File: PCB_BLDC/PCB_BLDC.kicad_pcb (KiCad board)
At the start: 2 copper layers, 181.9 x 138.4 mm, 61 parts, among them J10 Conn_01x06, J11 Conn_01x07, J12 Conn_01x06, J13 Conn_01x08, J16 Conn_01x08, J17 Conn_01x10, J8 VCC_Unregulated, J9 VCC_GND, Q1 IRF4905, SW1 Rotary_Encoder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

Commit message: Main: Finish PCB Routing Add Filled Zone Texts
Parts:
- moved C2 5.91 mm to (121.9, 152.4)
- moved C1 5.18 mm to (88.8, 152.3)
- moved C4 5.18 mm to (93.9, 152.3)
- moved D1 5.18 mm to (77.4, 152.2)
- moved L1 5.18 mm to (109.1, 145.6)
- moved R1 5.18 mm to (82.8, 153.8)
- moved Q1 5.18 mm to (55.1, 148.1)
- moved R2 5.18 mm to (71.7, 152.3)
- moved J8 4.83 mm to (32.0, 148.3)
- moved C3 3.97 mm to (136.3, 151.8)
- moved C5 3.97 mm to (158.5, 151.8)
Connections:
- A1 pad 5: /5V -> /VCC_5V
- A1 pad 8: /VCC_5V -> /VIN
- J11 pad 1: /L3_Sense -> /VCC_5V
- J11 pad 2: /L2_Sense -> /L3_Sense
- J11 pad 3: /L1_Sense -> /L2_Sense
- J11 pad 4: /VCC_5V -> /L1_Sense
- J13 pad 5: /5V -> /VCC_5V
- J13 pad 8: /VCC_5V -> /VIN
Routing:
- net /VCC_5V: track 159.8 -> 173.5 mm
- net /VCC_Filtered: track 314.1 -> 301.4 mm
- net /L1_Sense: track 158.8 -> 169.1 mm
- net /L2_Sense: track 153.4 -> 163.5 mm
- net /L3_Sense: track 147.8 -> 157.8 mm
- net /VIN: track 0.00 -> 5.00 mm
- net /5V: track 5.00 -> 0.00 mm
- net GND: track 133.7 -> 137.1 mm, vias 0 -> 86
- net /VCC_Polartiy_Check: track 62.6 -> 64.5 mm
- added copper zone on B.Cu, net GND
- added copper zone on F.Cu, net GND
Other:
- board text added: "1"
- board text added: "2"
- board text added: "3"
- board text added: "5V"
- board text added: "Current |"
- board text added: "GND"
- board text added: "Hall Sense"
- board text added: "L1"
- board text added: "L2"
- board text added: "L3"
- board text added: "VCC"

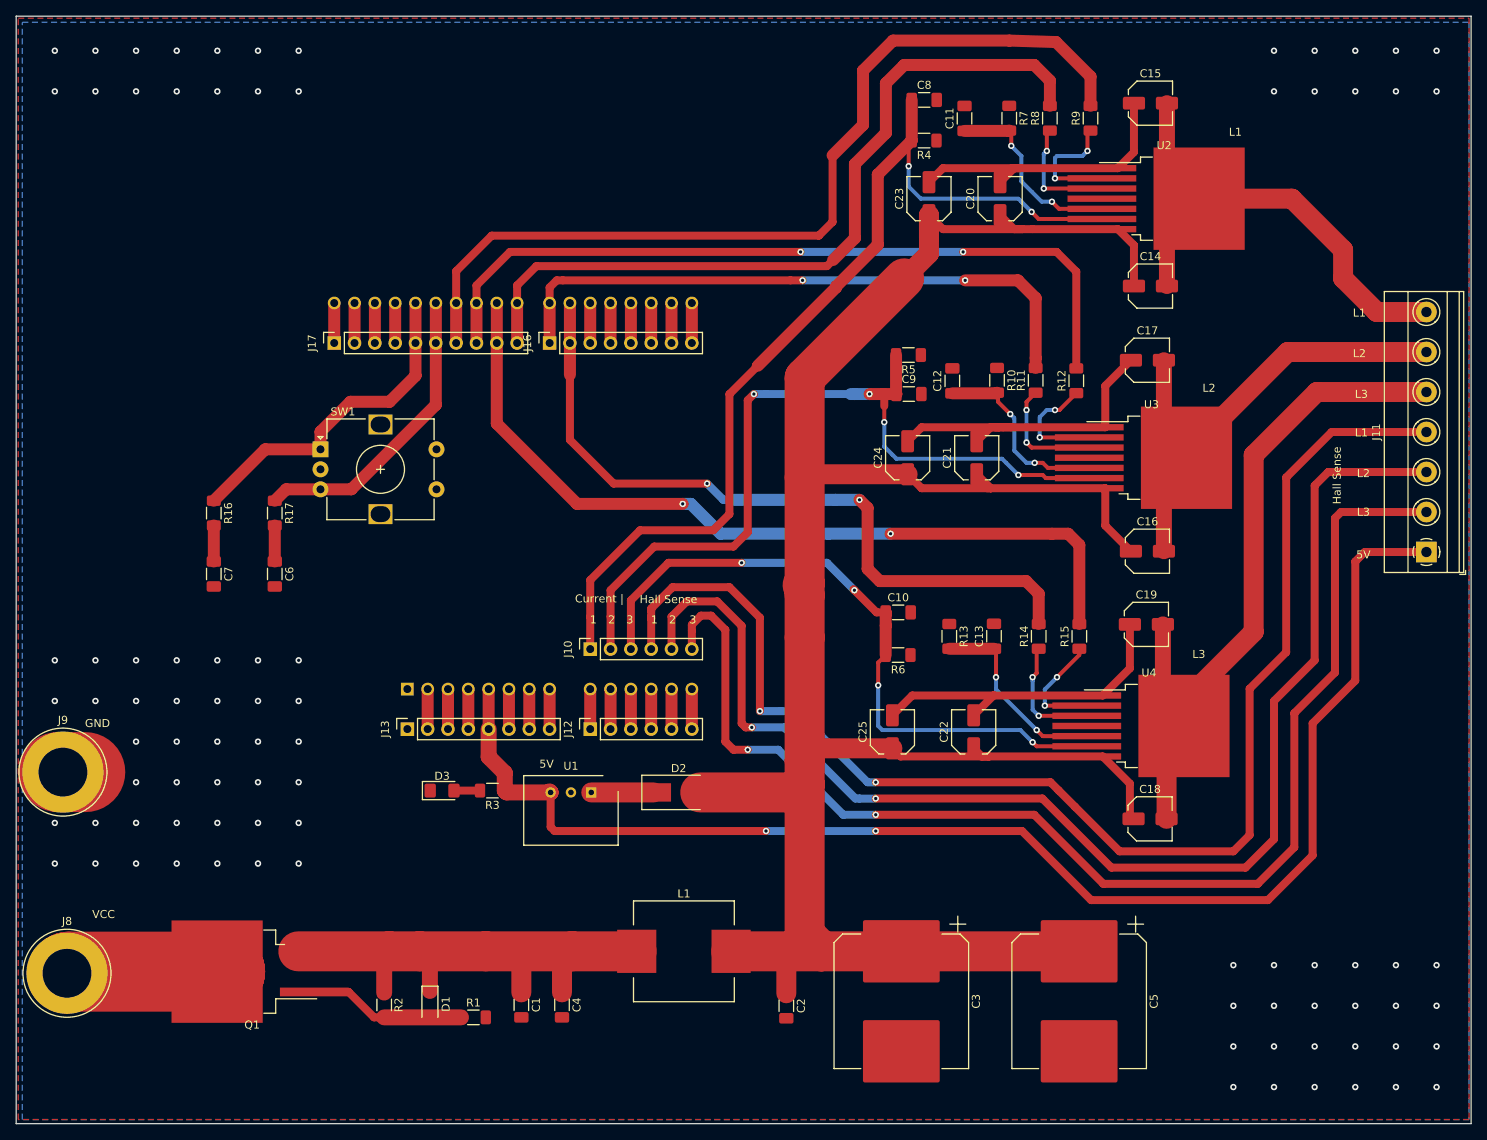
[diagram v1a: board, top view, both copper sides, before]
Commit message: Main: Add Text to Schematic and PCB, Images
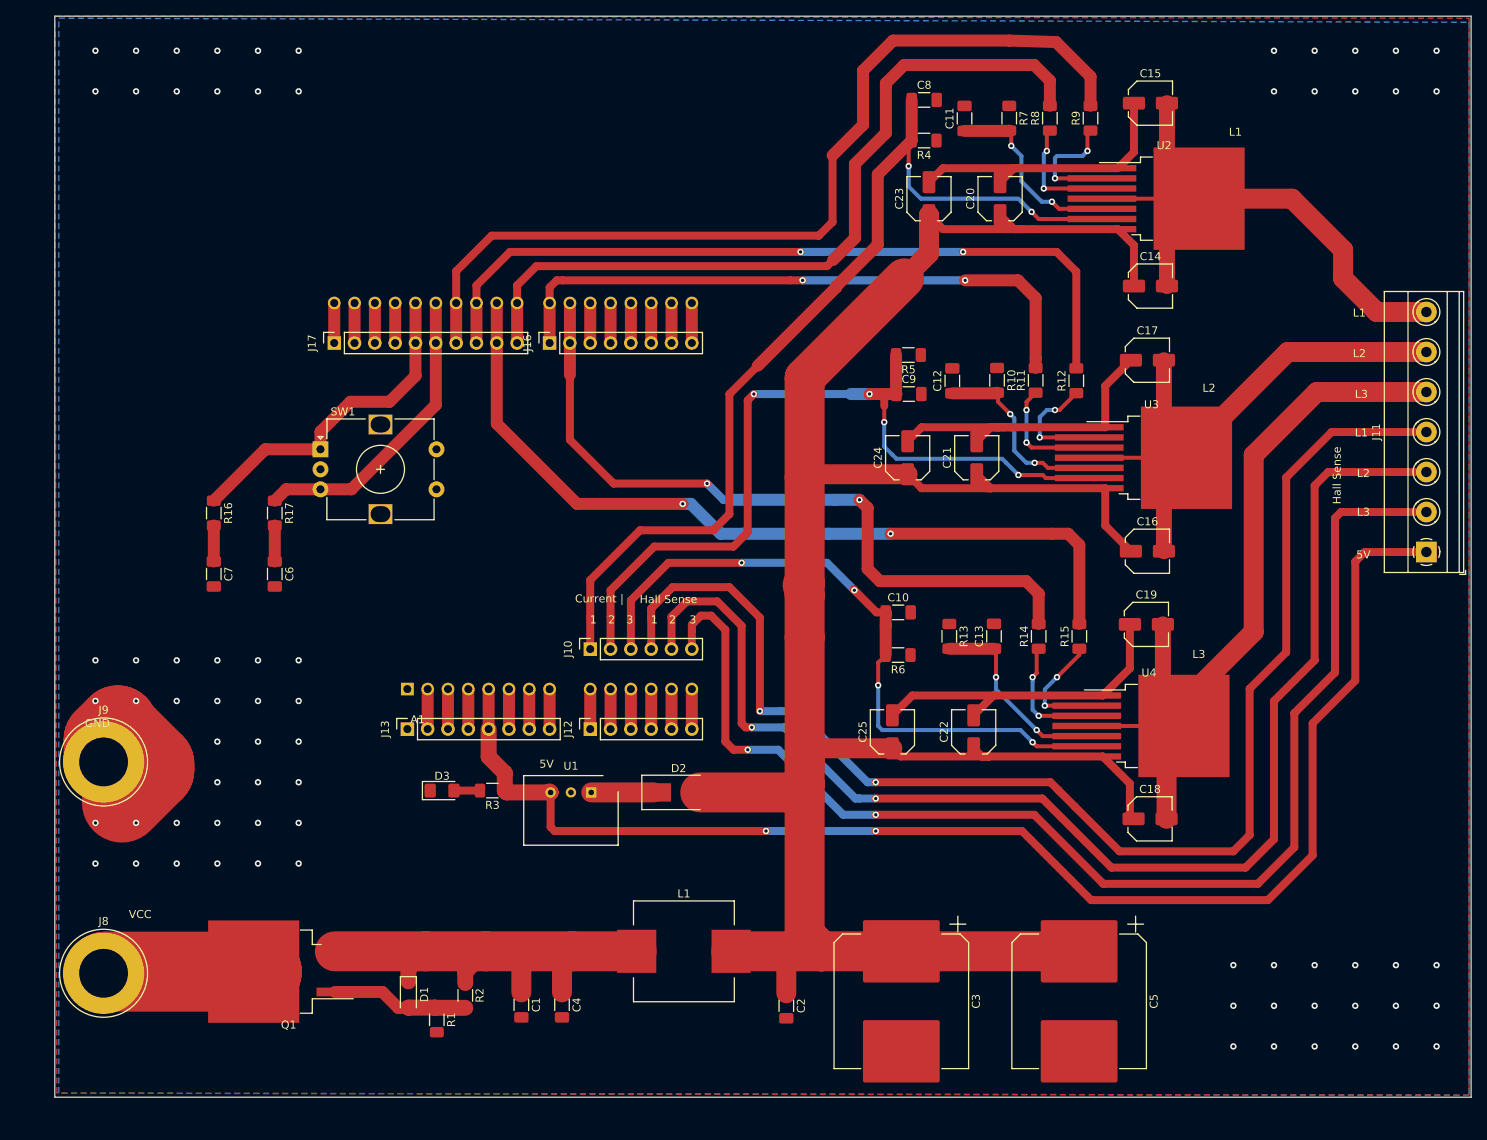
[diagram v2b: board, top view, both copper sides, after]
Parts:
- moved R2 10.2 mm to (81.8, 151.1)
- moved J9 5.24 mm to (36.6, 121.9)
- moved R1 4.58 mm to (78.2, 154.2), turned to 270 degrees
- moved J8 4.57 mm to (36.6, 148.3)
- moved Q1 4.57 mm to (59.7, 148.1)
- moved D1 2.95 mm to (74.7, 151.0)
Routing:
- net GND: track 137.1 -> 152.2 mm, vias 86 -> 70
- net /L3_Motor: track 96.8 -> 106.0 mm
- net /L2_Motor: track 61.9 -> 71.0 mm
- net /L1_Motor: track 66.3 -> 75.5 mm
- net /VCC_Polartiy_Check: track 64.5 -> 59.6 mm
- net Net-(D1-Pad2): track 21.7 -> 23.4 mm
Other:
- board size 181.9 x 138.4 mm -> 177 x 135.1 mm
